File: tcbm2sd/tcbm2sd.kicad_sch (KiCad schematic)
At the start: 27 parts, among them J1 TCBM, J2 JTAG, J4 AMS1117, J5 SD CARD, J7 ALT_A6_A7, SW1 BUT_PREV, SW2 BUT_NEXT, U1 XC9572XL-VQ64, U2 Arduino Pro Mini, U3 AMS1117-3.3, U4 27C512

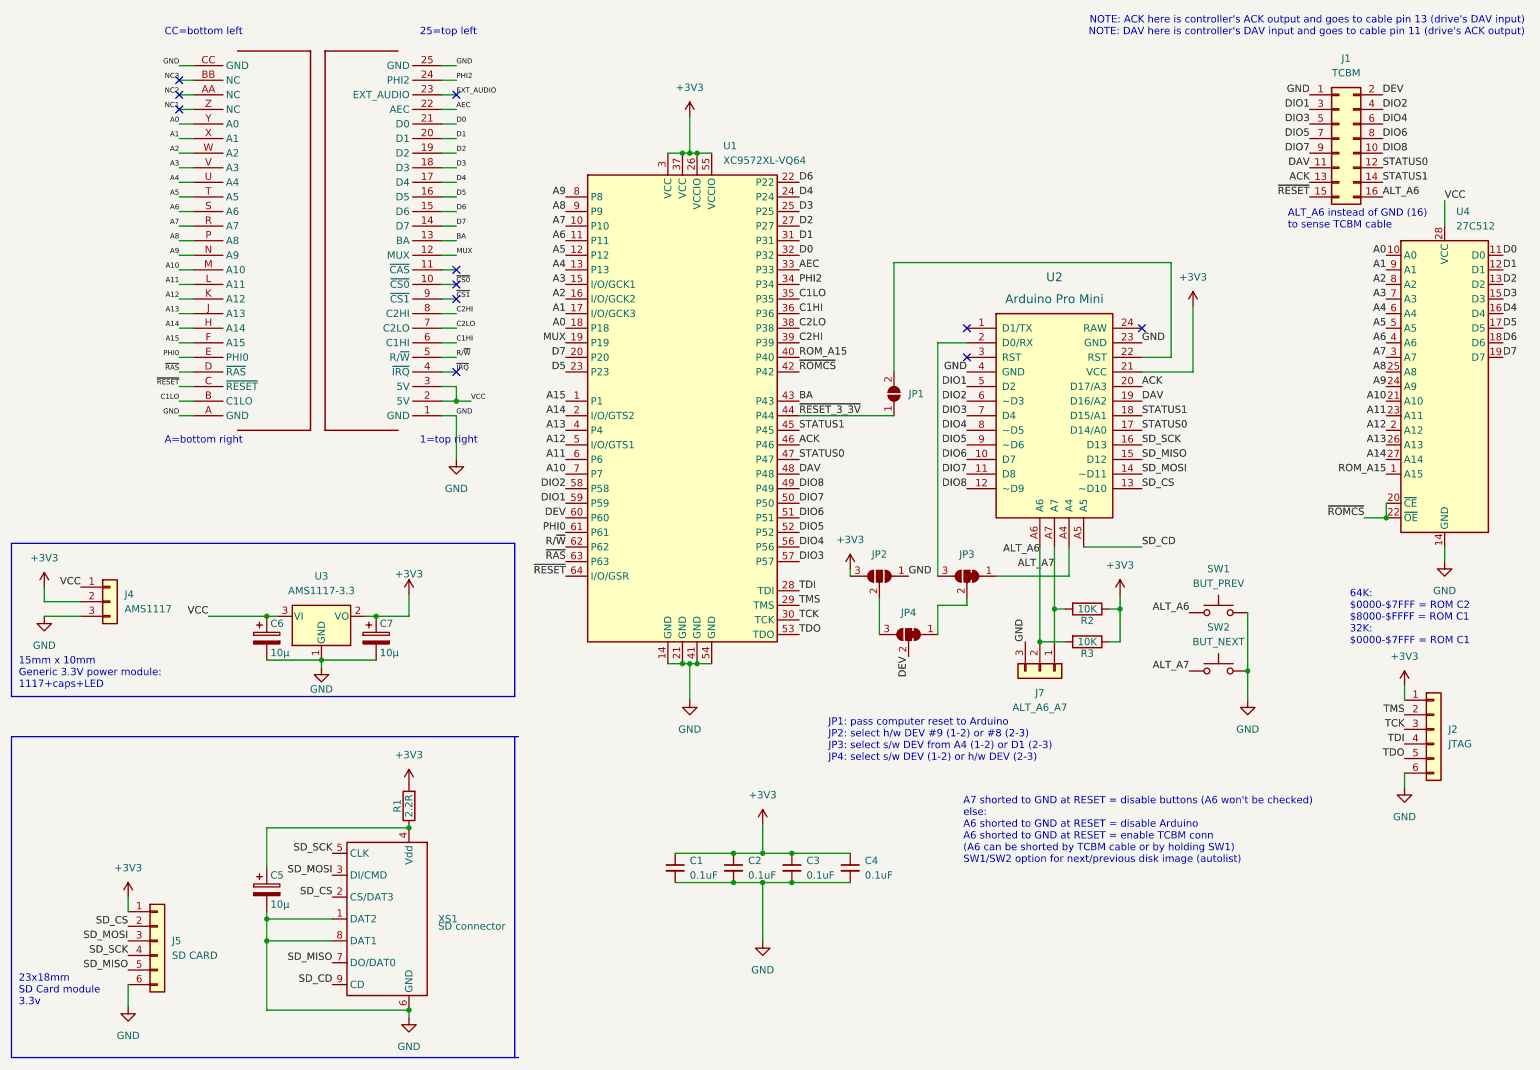
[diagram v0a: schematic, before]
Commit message: Switch to 44-pin connector
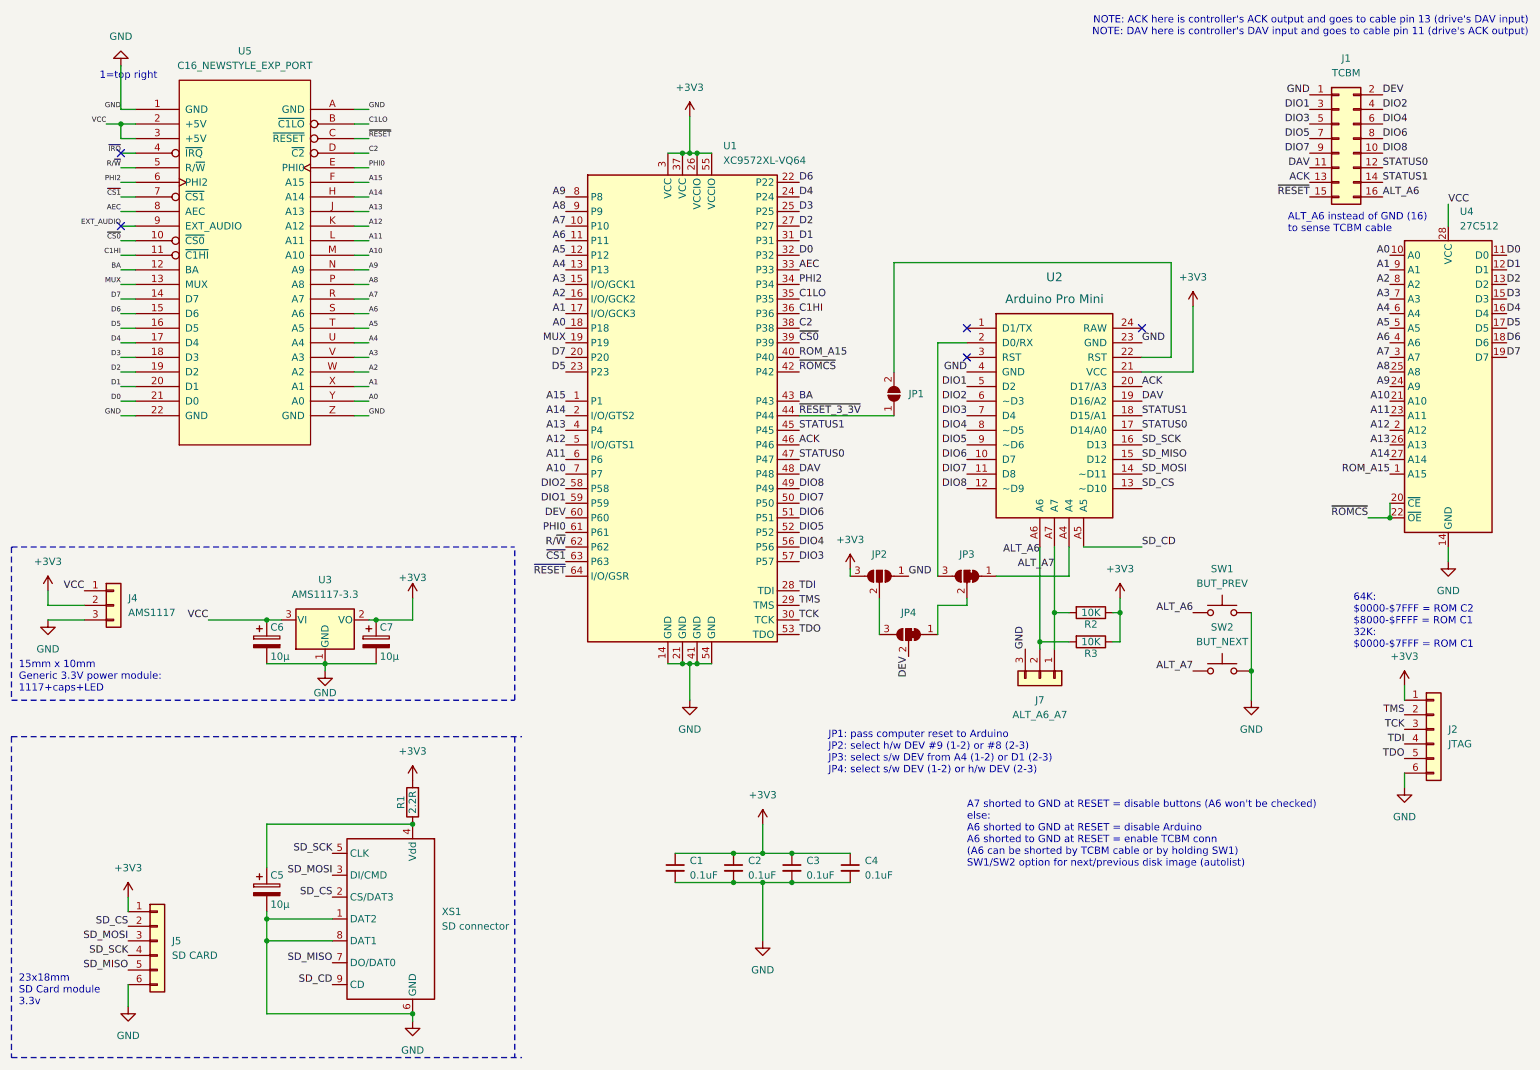
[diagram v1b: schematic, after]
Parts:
- removed U$1: C16_CARTRIDGE, c264-magic-cart-rev1:C16_CART, symbol tcbm2sd:C16_CARTRIDGE
- added U5: C16_NEWSTYLE_EXP_PORT, LittleSixteen:EdgeConn-44pin, symbol C16-Exp-Port-44pin-In:C16_NEWSTYLE_EXP_PORT
- XS1: symbol uSD_push-push_ebay:SD_ebay-uSD-push/push_SMD -> uSD_push-push_ebay:SD_ebay-uSD-push/push_SMD; Manf SHOU HAN -> ebay; Manf# TF-CARD H1.8 -> _
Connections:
- net C2HI is gone; now on net ~{CS0}: U1.39 (P39)
- net ~{RAS} is gone; now on net ~{CS1}: U1.63 (P63)
- net A0: now also U5.Y (A0)
- net A1: now also U5.X (A1)
- net A10: now also U5.M (A10)
- net A11: now also U5.L (A11)
- net A12: now also U5.K (A12)
- net A13: now also U5.J (A13)
- net A14: now also U5.H (A14)
- net A15: now also U5.F (A15)
- net A2: now also U5.W (A2)
- net A3: now also U5.V (A3)
- net A4: now also U5.U (A4)
- net A5: now also U5.T (A5)
- net A6: now also U5.S (A6)
- net A7: now also U5.R (A7)
- net A8: now also U5.P (A8)
- net A9: now also U5.N (A9)
- net AEC: now also U5.8 (AEC)
- net BA: now also U5.12 (BA)
- net C1HI: now also U5.11 (~{C1HI})
- net C1LO: now also U5.B (~{C1LO})
- net D0: now also U5.21 (D0)
- net D1: now also U5.20 (D1)
- net D2: now also U5.19 (D2)
- net D3: now also U5.18 (D3)
- net D4: now also U5.17 (D4)
- net D5: now also U5.16 (D5)
- net D6: now also U5.15 (D6)
- net D7: now also U5.14 (D7)
- net EXT_AUDIO: now also U5.9 (EXT_AUDIO)
- net GND: now also U5.1 (GND), U5.22 (GND), U5.A (GND), U5.Z (GND)
- net MUX: now also U5.13 (MUX)
- net PHI0: now also U5.E (PHI0)
- net PHI2: now also U5.6 (PHI2)
- net R/~{W}: now also U5.5 (R/~{W})
- net VCC: now also U5.2 (+5V), U5.3 (+5V)
- net ~{CS0}: now also U5.10 (~{CS0})
- net ~{CS1}: now also U5.7 (~{CS1})
- net ~{IRQ}: now also U5.4 (~{IRQ})
- net ~{RESET}: now also U5.C (~{RESET})
- net C2LO renamed C2
- net C2: now also U5.D (~{C2})
- no-connect marks 11 -> 5
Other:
- note removed: "25=top left"
- note removed: "A=bottom right"
- note removed: "CC=bottom left"
- moved on the sheet: C6, C7, J4, J7, R1, R2, R3, SW1, SW2, U3, U4, XS1
